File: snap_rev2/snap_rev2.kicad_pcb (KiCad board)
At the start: 2 copper layers, 60.4 x 22.1 mm, 29 parts, among them J1 Audio-Jack-4_1Switches, P1 CONN_02X05, Q1 TSM2301, SW1 SW_SPST, U1 TPS610986, U2 MDBT42Q, Y1 32786Hz

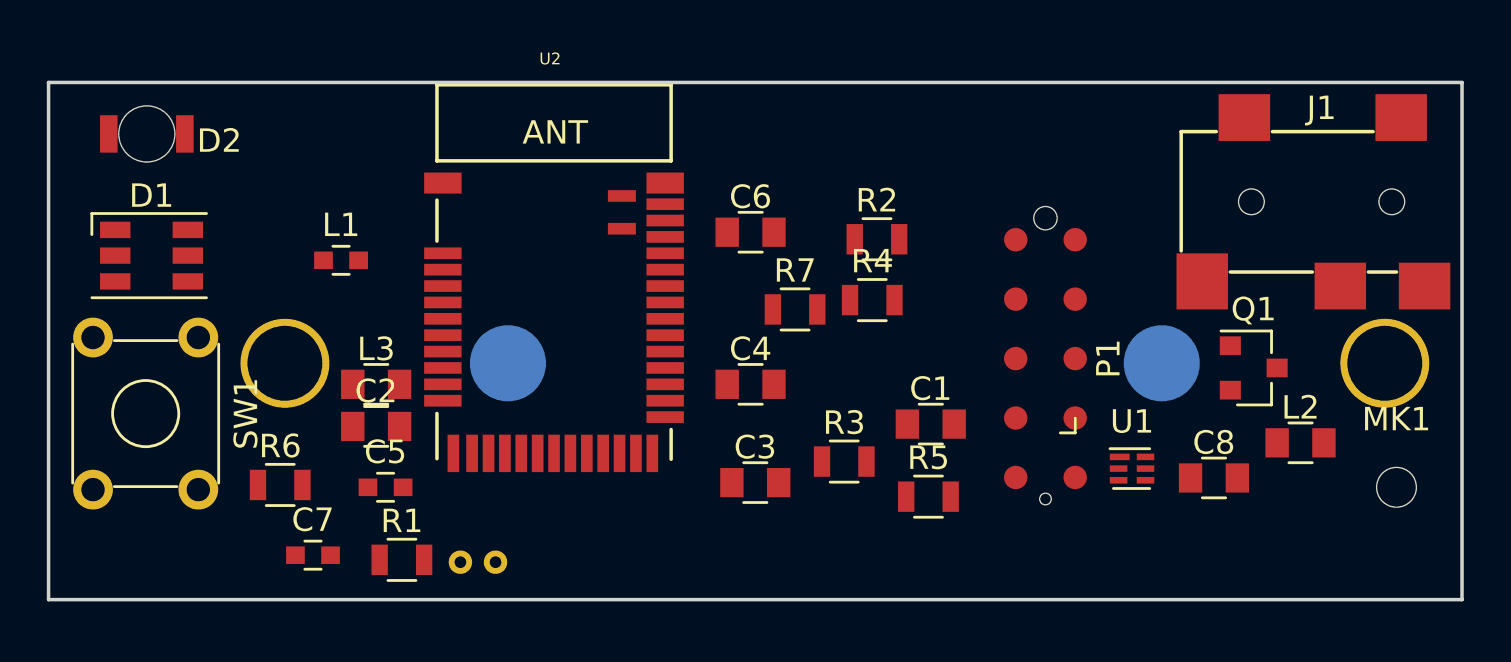
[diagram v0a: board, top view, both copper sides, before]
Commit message: Snap rev2 updated with SMD switch, 5050 LED and bigger crystal
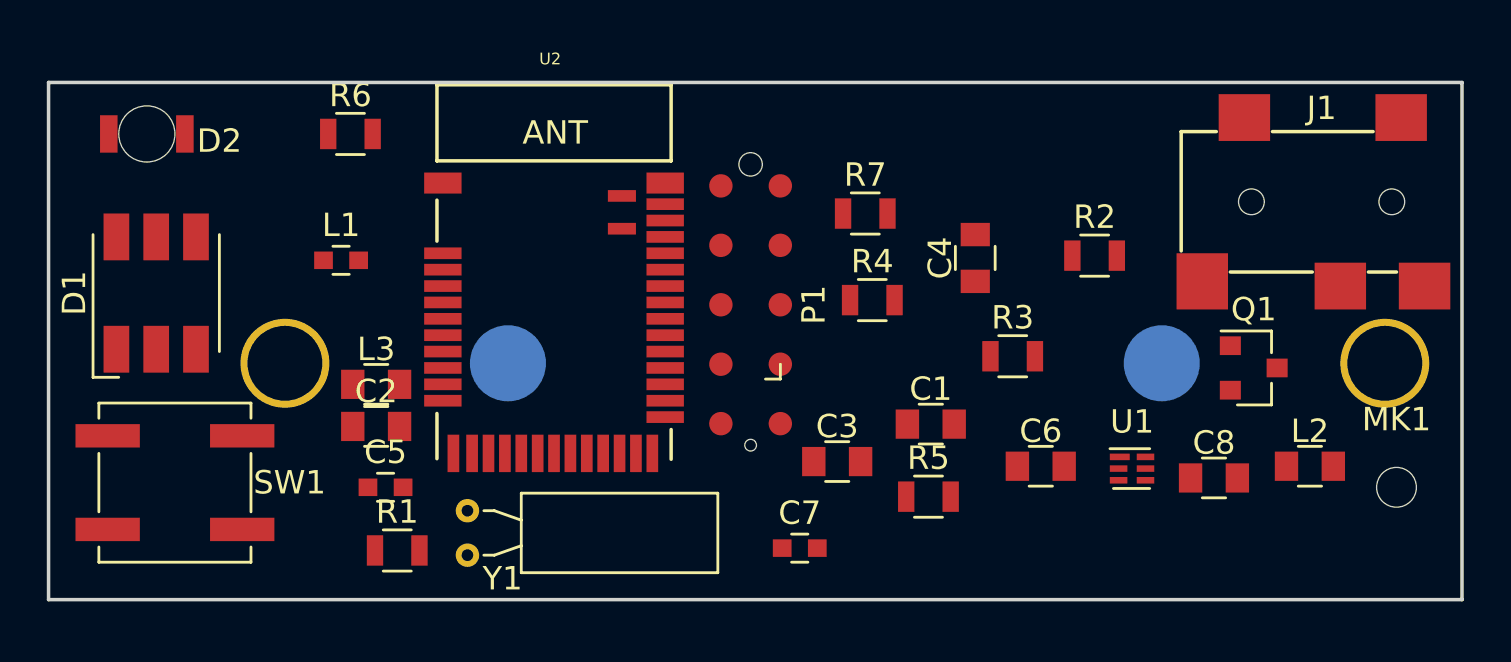
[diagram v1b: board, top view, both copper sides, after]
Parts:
- D1: value CLX6F-FKC -> 5050_RGB_LED; footprint LEDs:LED_RGB_PLCC-6 -> LEDs:LED_RGB_5050-6
- J1: value Audio-Jack-4_1Switches -> SJ2-35863B1
- R1: value 400 -> 400E
- R3: value 400 -> 390E
- R4: value 82 -> 82E
- R5: value 68 -> 68E
- R6: value 33 -> 33E
- R7: value 130 -> 130E
- SW1: value SW_SPST -> 1825910-6; footprint Buttons_Switches_THT:SW_TH_Tactile_Omron_B3F-10xx -> Buttons_Switches_SMD:SW_SPST_B3SL-1002P
- Y1: value 32786Hz -> ECS-3X8X; footprint Crystals:Crystal_DS10_d1.0mm_l4.3mm_Vertical -> Crystals:Crystal_C38-LF_d3.0mm_l8.0mm_Horizontal; moved to F.Cu
- moved C7 20.8 mm to (98.5, 107.9)
- moved C6 15.9 mm to (108.8, 104.4)
- moved R6 15.3 mm to (79.3, 90.2)
- moved P1 12.8 mm to (96.4, 97.5)
- moved C4 11.0 mm to (106.0, 95.5), turned to 90 degrees
- moved R2 9.33 mm to (111.1, 95.4)
- moved R3 8.49 mm to (107.6, 99.7)
- moved SW1 6.28 mm to (71.8, 105.1), turned to 0 degrees
- moved R7 5.08 mm to (101.3, 93.6)
- moved C3 3.61 mm to (100.1, 104.2)
- moved D1 1.61 mm to (71.0, 97.0), turned to 90 degrees
- moved L2 1.08 mm to (120.3, 104.4)
- moved R1 0.45 mm to (81.3, 108.0)
- moved Y1 0.42 mm to (84.3, 108.2), turned to 90 degrees
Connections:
- D1 pad 4: Net-(D1-Pad4) -> /LED_SENSE
- D1 pad 5: /LED_SENSE -> Net-(D1-Pad5)
- R5 pad 1: /LED_GREEN -> /LED_RED
- R5 pad 2: /LED_SENSE -> Net-(D1-Pad5)
- R6 pad 1: /LED_RED -> /LED_GREEN
- R6 pad 2: Net-(D1-Pad4) -> /LED_SENSE

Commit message: Optimized the PCB to 55x22 mm^2
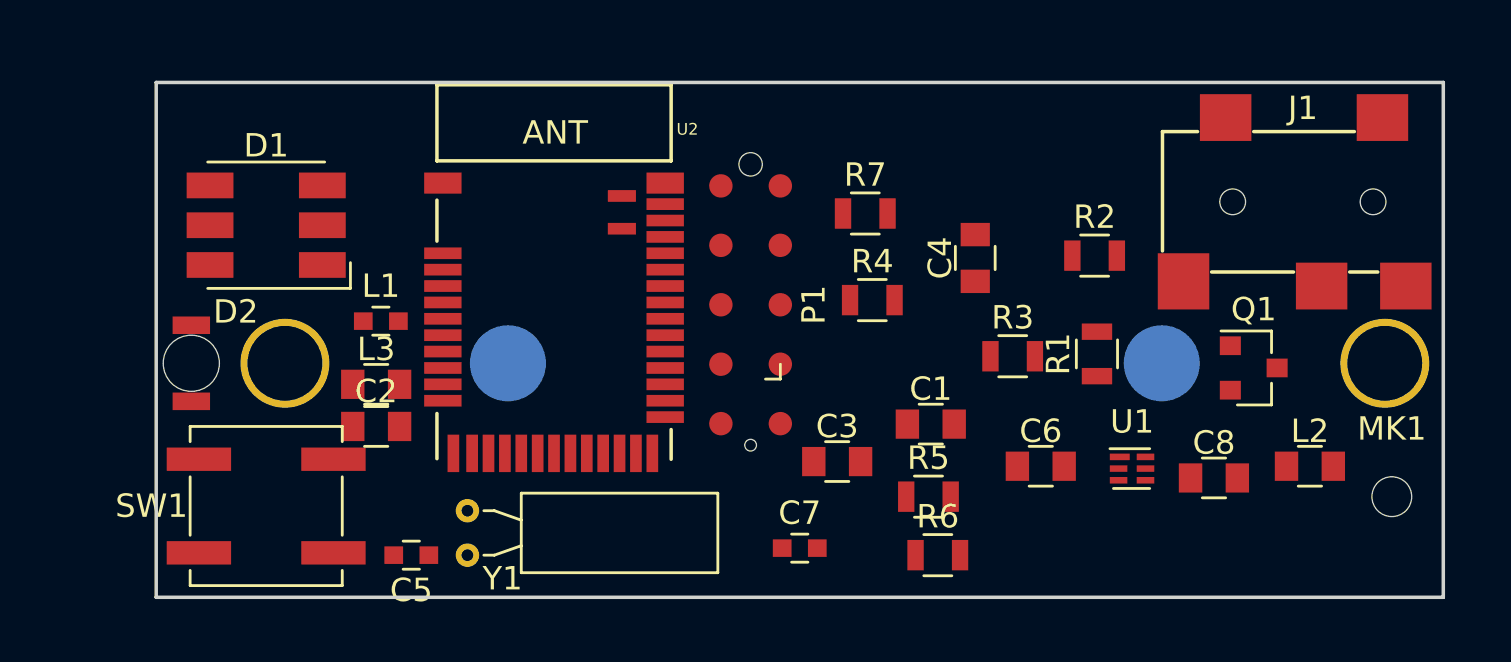
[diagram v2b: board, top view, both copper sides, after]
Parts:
- R1: value 400E -> 390E
- moved R1 31.1 mm to (111.2, 99.6), turned to 90 degrees
- moved R6 30.9 mm to (104.4, 108.2)
- moved D2 9.98 mm to (72.5, 100.0), turned to 270 degrees
- moved D1 5.52 mm to (75.7, 94.1), turned to 180 degrees
- moved SW1 4.03 mm to (75.7, 106.1), turned to 180 degrees
- moved L1 3.11 mm to (80.6, 98.2)
- moved C5 3.10 mm to (81.9, 108.2), turned to 180 degrees
- moved J1 0.80 mm to (126.0, 93.1)
- moved MK1 0.45 mm to (123.8, 105.7)
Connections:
- R5 pad 1: /LED_RED -> /LED_GREEN
- R5 pad 2: Net-(D1-Pad5) -> /LED_SENSE
- R6 pad 1: /LED_GREEN -> /LED_RED
- R6 pad 2: /LED_SENSE -> Net-(D1-Pad5)
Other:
- board size 60.4 x 22.1 mm -> 55 x 22 mm
- net class Default: trace_width 0.25 -> 0.2; via_dia 0.8 -> 0.65; via_drill 0.4 -> 0.25
- rule via_min_drill: 0.3 -> 0.25
- rule via_min_size: 0.4 -> 0.65
